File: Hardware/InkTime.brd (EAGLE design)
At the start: 46 x 35 mm, 105 parts, among them IC1 BQ25180YBGR, IC2 DRV2605YZFR, IC3 BMA423, IC9 RT6160AWSC, J1 503480-2400, J2 TC2030-IDC, J4 KH-TYPE-C-16P, Q1 20V/4.2A/52mΩ/1.4W, Q3 SI1308EDL-T1-GE3, U1 NRF52840_QF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

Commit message: fix: BMA423 -> BMA421
Signed-off-by: Luca Mazilescu <luca.mazilescu@protonmail.com>
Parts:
- IC3: value BMA423 -> BMA421
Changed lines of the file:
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@@
 <layers>
 <layer number="1" name="Top" color="4" fill="1" visible="yes" active="yes"/>
-<layer number="2" name="Route2" color="16" fill="1" visible="no" active="yes"/>
+<layer number="2" name="Route2" color="16" fill="1" visible="yes" active="yes"/>
 <layer number="3" name="Route3" color="17" fill="1" visible="no" active="no"/>
 <layer number="4" name="Route4" color="18" fill="1" visible="no" active="no"/>
@@
 <layer number="13" name="Route13" color="21" fill="1" visible="no" active="no"/>
 <layer number="14" name="Route14" color="22" fill="1" visible="no" active="no"/>
-<layer number="15" name="Route15" color="23" fill="1" visible="no" active="yes"/>
-<layer number="16" name="Bottom" color="1" fill="1" visible="no" active="yes"/>
-<layer number="17" name="Pads" color="2" fill="1" visible="no" active="yes"/>
-<layer number="18" name="Vias" color="2" fill="1" visible="no" active="yes"/>
-<layer number="19" name="Unrouted" color="6" fill="1" visible="no" active="yes"/>
-<layer number="20" name="Dimension" color="24" fill="1" visible="no" active="yes"/>
+<layer number="15" name="Route15" color="23" fill="1" visible="yes" active="yes"/>
+<layer number="16" name="Bottom" color="1" fill="1" visible="yes" active="yes"/>
+<layer number="17" name="Pads" color="2" fill="1" visible="yes" active="yes"/>
+<layer number="18" name="Vias" color="2" fill="1" visible="yes" active="yes"/>
+<layer number="19" name="Unrouted" color="6" fill="1" visible="yes" active="yes"/>
+<layer number="20" name="Dimension" color="24" fill="1" visible="yes" active="yes"/>
 <layer number="21" name="tPlace" color="7" fill="1" visible="yes" active="yes"/>
-<layer number="22" name="bPlace" color="7" fill="1" visible="no" active="yes"/>
+<layer number="22" name="bPlace" color="7" fill="1" visible="yes" active="yes"/>
 <layer number="23" name="tOrigins" color="15" fill="1" visible="yes" active="yes"/>
 <layer number="24" name="bOrigins" color="15" fill="1" visible="yes" active="yes"/>
 <layer number="25" name="tNames" color="7" fill="1" visible="yes" active="yes"/>
-<layer number="26" name="bNames" color="7" fill="1" visible="no" active="yes"/>
+<layer number="26" name="bNames" color="7" fill="1" visible="yes" active="yes"/>
 <layer number="27" name="tValues" color="7" fill="1" visible="no" active="yes"/>
 <layer number="28" name="bValues" color="7" fill="1" visible="no" active="yes"/>
-<layer number="29" name="tStop" color="7" fill="3" visible="yes" active="yes"/>
+<layer number="29" name="tStop" color="7" fill="3" visible="no" active="yes"/>
 <layer number="30" name="bStop" color="7" fill="6" visible="no" active="yes"/>
 <layer number="31" name="tCream" color="7" fill="4" visible="no" active="yes"/>
@@
 <layer number="37" name="tTest" color="7" fill="1" visible="no" active="yes"/>
 <layer number="38" name="bTest" color="7" fill="1" visible="no" active="yes"/>
-<layer number="39" name="tKeepout" color="4" fill="11" visible="no" active="yes"/>
-<layer number="40" name="bKeepout" color="1" fill="11" visible="no" active="yes"/>
-<layer number="41" name="tRestrict" color="4" fill="10" visible="no" active="yes"/>
-<layer number="42" name="bRestrict" color="1" fill="10" visible="no" active="yes"/>
+<layer number="39" name="tKeepout" color="4" fill="11" visible="yes" active="yes"/>
+<layer number="40" name="bKeepout" color="1" fill="11" visible="yes" active="yes"/>
+<layer number="41" name="tRestrict" color="4" fill="10" visible="yes" active="yes"/>
+<layer number="42" name="bRestrict" color="1" fill="10" visible="yes" active="yes"/>
 <layer number="43" name="vRestrict" color="2" fill="10" visible="no" active="yes"/>
 <layer number="44" name="Drills" color="7" fill="1" visible="no" active="yes"/>
@@
 <layer number="49" name="Reference" color="7" fill="1" visible="no" active="yes"/>
 <layer number="50" name="dxf" color="7" fill="1" visible="no" active="no"/>
-<layer number="51" name="tDocu" color="7" fill="1" visible="no" active="yes"/>
-<layer number="52" name="bDocu" color="7" fill="1" visible="no" active="yes"/>
+<layer number="51" name="tDocu" color="7" fill="1" visible="yes" active="yes"/>
+<layer number="52" name="bDocu" color="7" fill="1" visible="yes" active="yes"/>
 <layer number="53" name="tGND_GNDA" color="7" fill="1" visible="no" active="no"/>
 <layer number="54" name="bGND_GNDA" color="7" fill="1" visible="no" active="no"/>
@@
 <attribute name="VALUE" x="18" y="15.94" size="1.27" layer="27" align="center"/>
 </element>
-<element name="IC3" library="InkTime_v5" library_urn="urn:adsk.wipprod:fs.file:vf.8BTbcW1WSFWj7_HBs_dgew" package="BMA423_BMA423" value="BMA423" x="-17.7" y="-12.2" smashed="yes">
+<element name="IC3" library="InkTime_v5" library_urn="urn:adsk.wipprod:fs.file:vf.8BTbcW1WSFWj7_HBs_dgew" package="BMA423_BMA423" value="BMA421" x="-17.7" y="-12.2" smashed="yes">
 <attribute name="ARROW_PART_NUMBER" value="BMA423" x="-17.7" y="-12.2" size="1.778" layer="27" display="off"/>
 <attribute name="ARROW_PRICE-STOCK" value="https://www.arrow.com/en/products/bma423/bosch" x="-17.7" y="-12.2" size="1.778" layer="27" display="off"/>

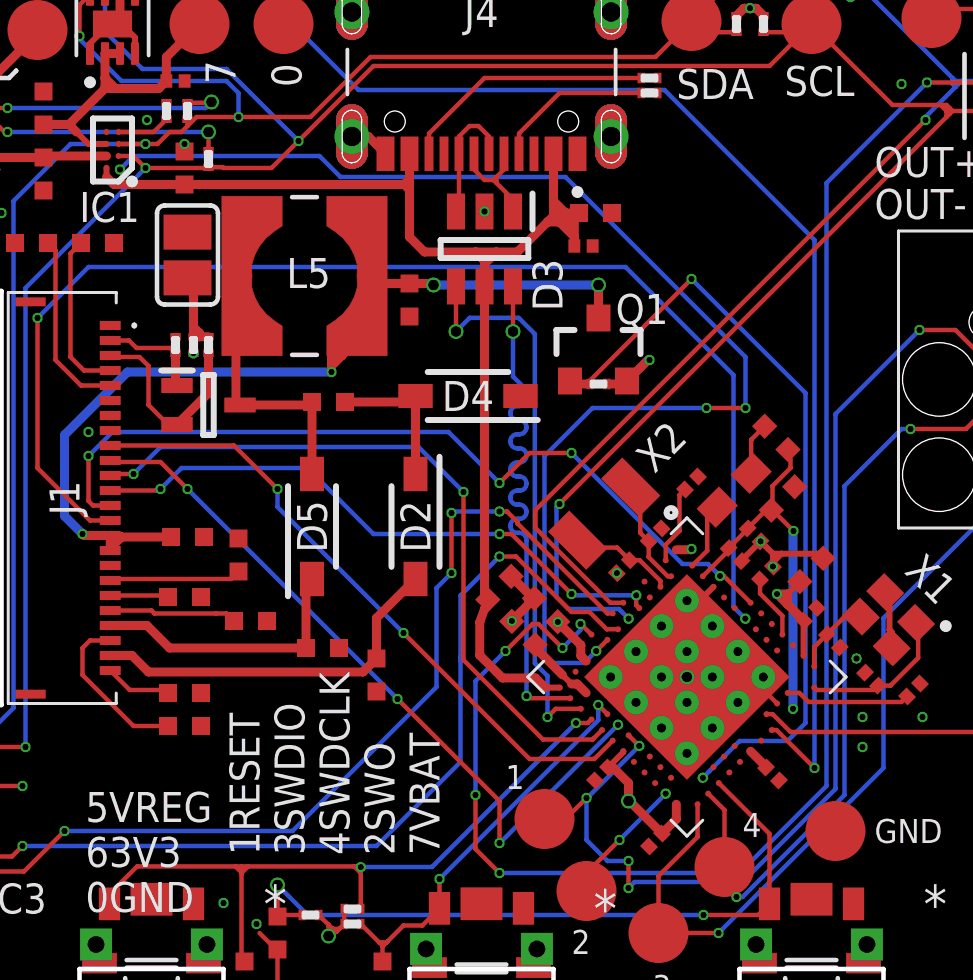
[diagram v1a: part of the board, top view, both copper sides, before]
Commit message: fix: mask P0.19 from nRF package
Signed-off-by: Luca Mazilescu <luca.mazilescu@protonmail.com>
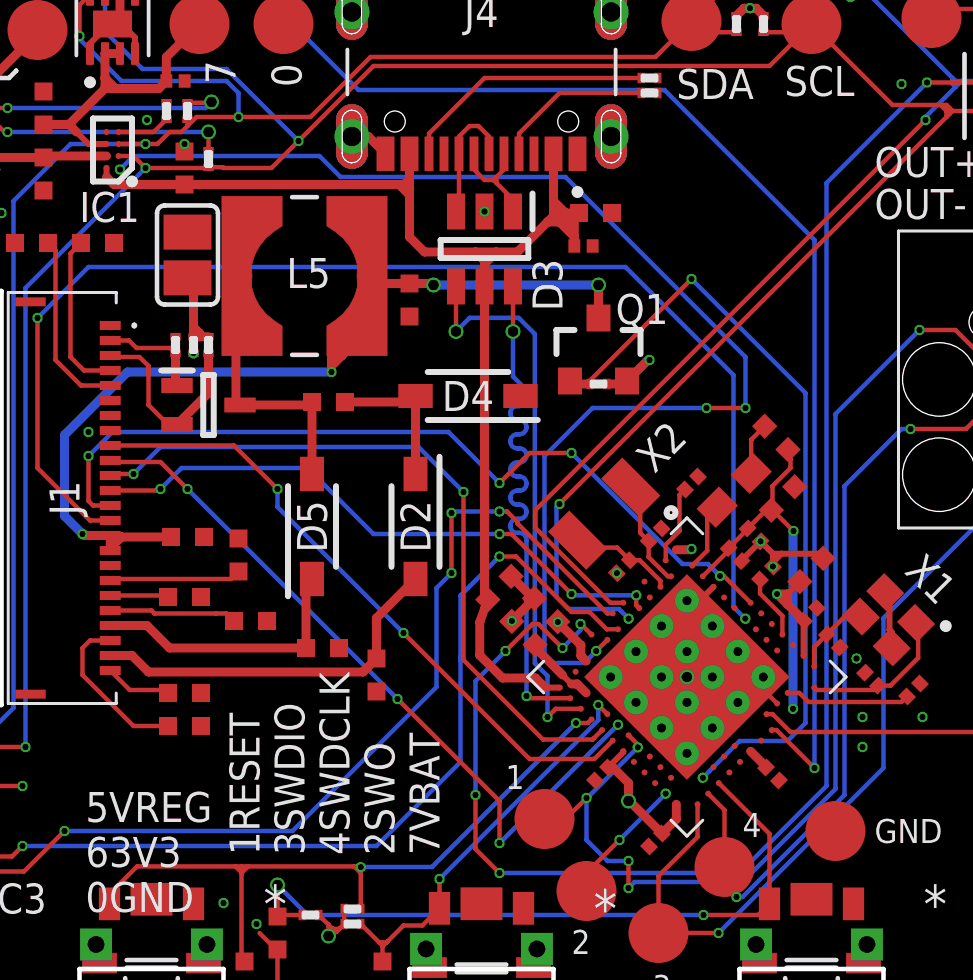
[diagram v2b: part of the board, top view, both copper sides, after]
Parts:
- U1: device InkTime_v5:NORDIC_NRF_4_AQFN50P700X700X85_HS-74N_PINCLEAN -> InkTime_v5:NORDIC_NRF_4_AQFN50P700X700X85_HS-74N_PINCLEAN2
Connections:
- net RESET: no longer U1.P$AC15
